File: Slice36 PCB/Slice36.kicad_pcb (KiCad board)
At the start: 2 copper layers, 118.8 x 97.2 mm, 52 parts, among them J1 AudioJack4, J2 AudioJack4, Sw1 choc_v1_dbl, Sw10 choc_v1_dbl, Sw11 choc_v1_dbl, Sw12 choc_v1_dbl, Sw13 choc_v1_dbl, Sw14 choc_v1_dbl, Sw15 choc_v1_dbl, Sw16 choc_v1_dbl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

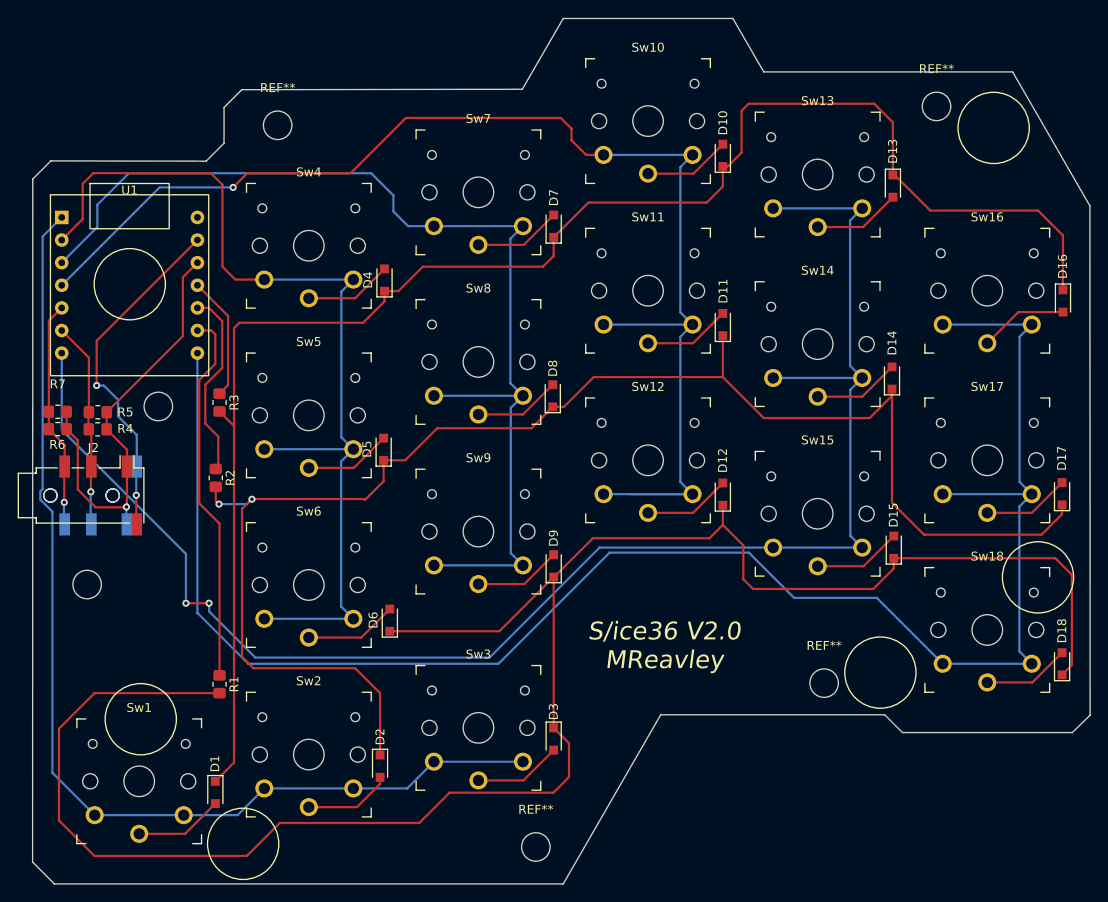
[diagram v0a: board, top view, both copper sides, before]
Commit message: Tightened up the edges, rounded the corners
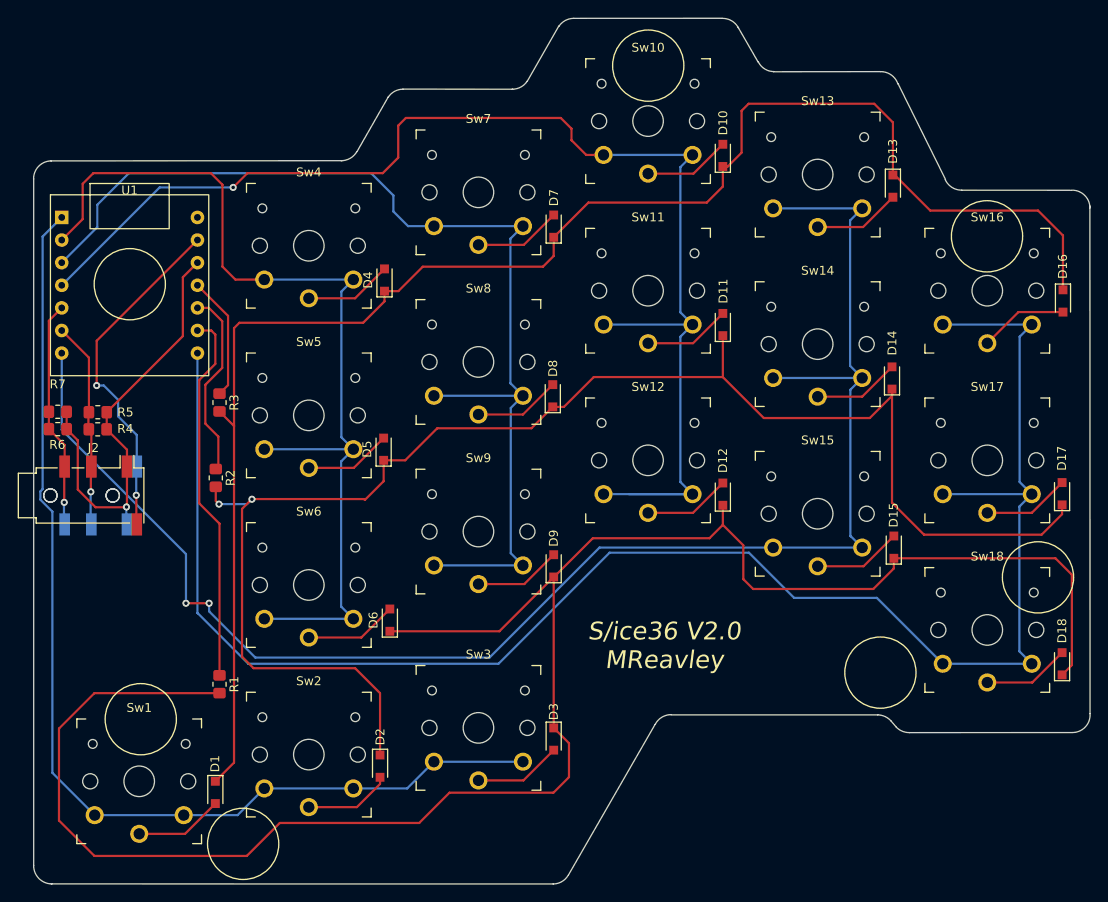
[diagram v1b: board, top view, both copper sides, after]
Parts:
- removed REF** (x6): MountingHole_3.2mm_M3, MountingHole:MountingHole_3.2mm_M3
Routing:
- net Net-(Sw10-Pad2): track 148.6 -> 150.7 mm
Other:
- board size 118.8 x 97.2 mm -> 118.7 x 97.2 mm
